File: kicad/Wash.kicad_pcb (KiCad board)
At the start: 4 copper layers, 55 x 35 mm, 40 parts, among them X2Y-CAN 4.7nF X2Y, X2Y-RS485 4.7nF X2Y

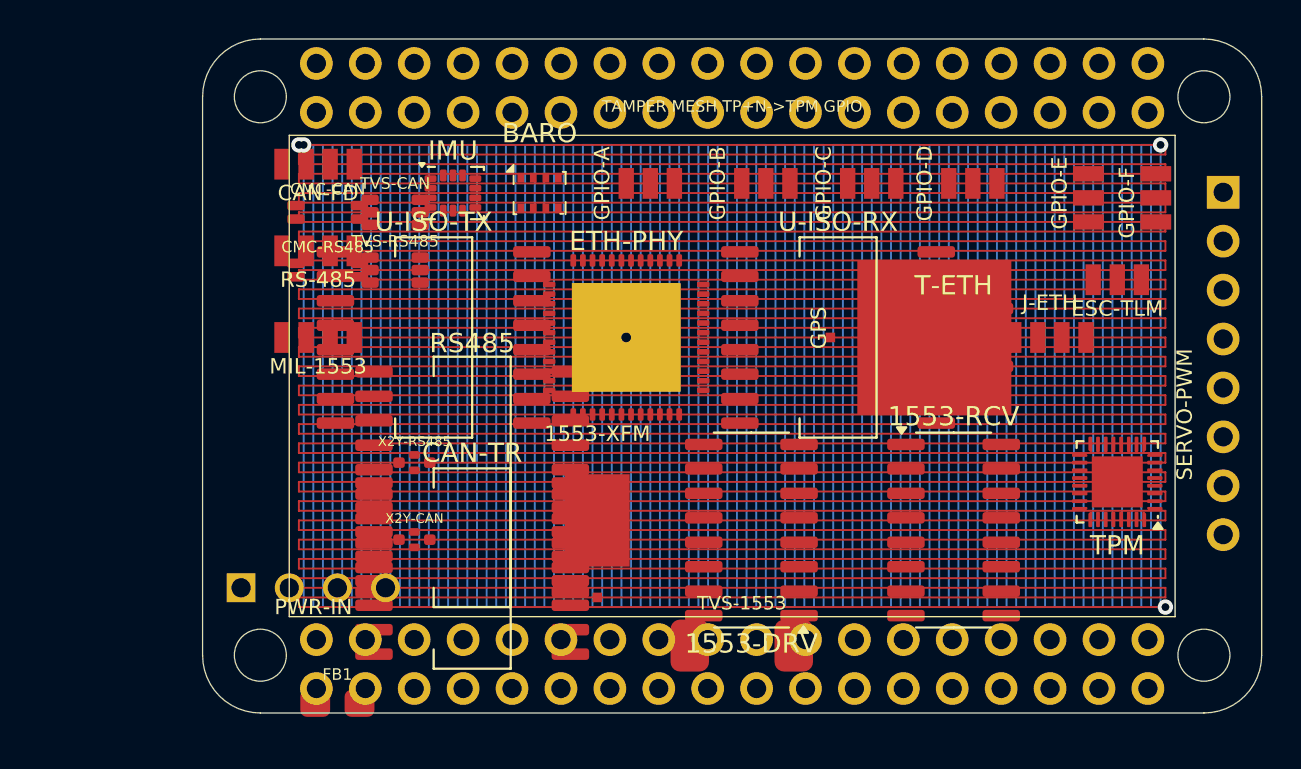
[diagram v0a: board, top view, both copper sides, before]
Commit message: avionics: wire second Ethernet (ETH2) on Wash; preserve Wash/Zoë layout work
Wash cape now carries a fully-wired second Ethernet channel.  The newly
placed ETH2 / ETH2-PHY (ADIN1300) / T-ETH2 (749010012A) footprints were
unconnected; this assigns their nets to mirror the ETH1 topology exactly:

  ETH2 (JST-GH-4P) --ETH2_LINE_{TX,RX}{P,N}--> T-ETH2 --ETH2_{TX,RX}{P,N}-->
  ETH2-PHY, reusing the host-side nets already broken out on the PB2-P2
  header (RMII1_* bus, shared MDIO/MDC, PHY2_INTRN/PHY2_RSTN, VCC2_ETH/
  GND/GND2_ETH).  44 pads assigned across the three parts (ETH2-PHY 32,
  T-ETH2 8, ETH2 4); diff-pair chains verified end to end.

Also preserves the manual component rearrangements on Wash and Zoë
(components reseated clear of the isolation moats).

Known follow-up (not in this commit): both PHYs share MDIO with no
address-strap resistors on the board (same default MDIO address); the
tamper-mesh shorts, ratsnest routing, and remaining DRC violations on all
four capes are still open.

Co-Authored-By: Claude Opus 4.8 <noreply@anthropic.com>
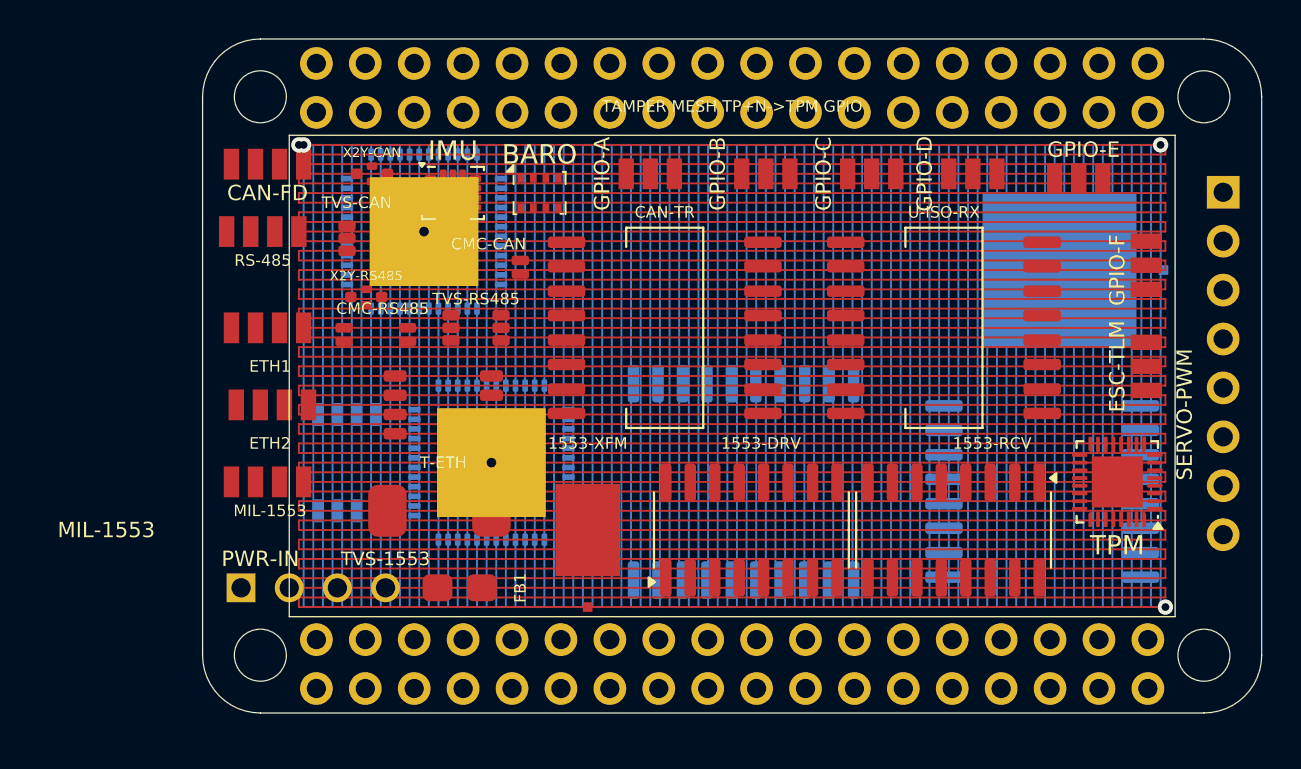
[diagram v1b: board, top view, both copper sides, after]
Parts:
- added ETH2: JST-GH-4P-ETH, JST_GH_4P, F.Cu at (124.6, 106.5)
- added ETH2-PHY: ADIN1300BCPZ, QFN-48-1EP_7x7mm_P0.5mm_EP5.65x5.65mm, B.Cu at (136.0, 109.5)
- added T-ETH2: 749010012A, ETH_XFMR_8P_5x3.5mm, B.Cu at (128.5, 109.5)
- ETH1-PHY: renamed from ETH-PHY; moved to B.Cu
- GPS, RS485, U-ISO-TX: moved to B.Cu
- moved ETH1 40.6 mm to (124.4, 102.5)
- moved U-ISO-TX 32.6 mm to (164.6, 111.0), turned to 180 degrees
- moved T-ETH 26.7 mm to (133.5, 106.5)
- moved X2Y-CAN 19.1 mm to (129.8, 94.5)
- moved TVS-1553 17.2 mm to (133.3, 112.0)
- moved CAN-TR 16.0 mm to (145.0, 102.5)
- moved RS485 14.1 mm to (149.1, 110.5), turned to -90 degrees
- moved ETH1-PHY 11.9 mm to (132.5, 97.5), turned to 180 degrees
- moved X2Y-RS485 8.96 mm to (129.5, 100.9)
- moved CMC-CAN 8.82 mm to (135.8, 99.3)
- moved FB1 8.74 mm to (134.3, 116.0)
- moved MIL-1553 7.95 mm to (124.4, 110.5)
- moved GPS 7.38 mm to (165.5, 99.5), turned to 180 degrees
- moved U-ISO-RX 5.52 mm to (159.5, 102.5)
- moved TVS-RS485 5.16 mm to (135.2, 102.5)
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- renumbered J-ETH to ETH1
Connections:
- CAN-TR pad 12: GND2_CAN -> (no net)
- CAN-TR pad 13: GND2_CAN -> (no net)
- CAN-TR pad 14: VCC2_CAN -> (no net)
- CAN-TR pad 9: CAN_H -> (no net)
- RS485 pad 11: VCC2_RS485 -> (no net)
- RS485 pad 12: GND2_RS485 -> (no net)
- RS485 pad 13: GND2_RS485 -> (no net)
- RS485 pad 14: RS485_A -> (no net)
- RS485 pad 18: GND2_RS485 -> (no net)
- RS485 pad 19: GND2_RS485 -> (no net)
- RS485 pad 20: VCC2_RS485 -> (no net)
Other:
- board text added: "MIL-1553"

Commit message: avionics(Wash): split PHY MDIO buses and wire field connectors
MDIO separation — each PB2-I NIC now manages its own PHY:
  * PHY1/ETH1-PHY -> MDIO0/MDC0 (CPSW MDIO, PB2-P2 pins 17/18)
  * PHY2/ETH2-PHY -> MDIO1/MDC1 (2nd bus, PB2-P2 pins 1/2 = spare SERVO6/7)
Removes the shared-MDIO same-address conflict (no strap needed). PCB pad
nets and schematic global labels both updated. PHY2's bus is a 2nd
(bit-banged mdio-gpio) MDIO — confirm the two balls are GPIO-capable in
the PB2-I pinmux and bring it up in the device tree.

Field connectors were all floating; wired each to its Description pinout:
  * SERVO-PWM pads 1-6 -> SERVO0-5 (servo PWM)
  * ESC-TLM -> GND / UART_ESC_TX / UART_ESC_RX
  * GPIO-A..F -> GND / +3V3 (+ GPIO_EXP_* signal pin labelled)
  * CAN-FD -> GND / CAN_H / CAN_L / +3V3
  * RS-485 -> GND / RS485_A / RS485_B / +3V3
  * PWR-IN -> +5V / +5V / GND / GND

The connector-vs-TMESH shorts DRC now reports are the pre-existing
tamper-mesh overlap (resolved by the per-domain mesh rework), not the
connector wiring.

Still open (need decisions, tracked in TODO 1.2a.1): source the 6
GPIO_EXP_A..F signals (PB2 header is full); add an ESC-PWM connector for
DSHOT0-3 (none on the PCB); wire MIL-1553 connector + transformer;
reconcile Wash.md §14 with the actual PCB connector set.

Co-Authored-By: Claude Opus 4.8 <noreply@anthropic.com>
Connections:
- CAN-FD pad 1: (no net) -> GND
- CAN-FD pad 2: (no net) -> CAN_H
- CAN-FD pad 3: (no net) -> CAN_L
- CAN-FD pad 4: (no net) -> +3V3
- ESC-TLM pad 1: (no net) -> GND
- ESC-TLM pad 2: (no net) -> UART_ESC_TX
- ESC-TLM pad 3: (no net) -> UART_ESC_RX
- ETH1-PHY pad 18: MDIO -> MDIO0
- ETH1-PHY pad 19: MDC -> MDC0
- ETH2-PHY pad 18: MDIO -> MDIO1
- ETH2-PHY pad 19: MDC -> MDC1
- GPIO-A pad 1: (no net) -> GND
- GPIO-A pad 2: (no net) -> +3V3
- GPIO-A pad 3: (no net) -> GPIO_EXP_A
- GPIO-B pad 1: (no net) -> GND
- GPIO-B pad 2: (no net) -> +3V3
- GPIO-B pad 3: (no net) -> GPIO_EXP_B
- GPIO-C pad 1: (no net) -> GND
- GPIO-C pad 2: (no net) -> +3V3
- GPIO-C pad 3: (no net) -> GPIO_EXP_C
- GPIO-D pad 1: (no net) -> GND
- GPIO-D pad 2: (no net) -> +3V3
- GPIO-D pad 3: (no net) -> GPIO_EXP_D
- GPIO-E pad 1: (no net) -> GND
- GPIO-E pad 2: (no net) -> +3V3
- GPIO-E pad 3: (no net) -> GPIO_EXP_E
- GPIO-F pad 1: (no net) -> GND
- GPIO-F pad 2: (no net) -> +3V3
- GPIO-F pad 3: (no net) -> GPIO_EXP_F
- PB2-P2 pad 1: SERVO7 -> MDIO1
- PB2-P2 pad 17: MDIO -> MDIO0
- PB2-P2 pad 18: MDC -> MDC0
- PB2-P2 pad 2: SERVO6 -> MDC1
- PWR-IN pad 1: (no net) -> +5V
- PWR-IN pad 2: (no net) -> +5V
- PWR-IN pad 3: (no net) -> GND
- PWR-IN pad 4: (no net) -> GND
- RS-485 pad 1: (no net) -> GND
- RS-485 pad 2: (no net) -> RS485_A
- RS-485 pad 3: (no net) -> RS485_B
- RS-485 pad 4: (no net) -> +3V3
- SERVO-PWM pad 1: (no net) -> SERVO0
- SERVO-PWM pad 2: (no net) -> SERVO1
- SERVO-PWM pad 3: (no net) -> SERVO2
- SERVO-PWM pad 4: (no net) -> SERVO3
- SERVO-PWM pad 5: (no net) -> SERVO4
- SERVO-PWM pad 6: (no net) -> SERVO5

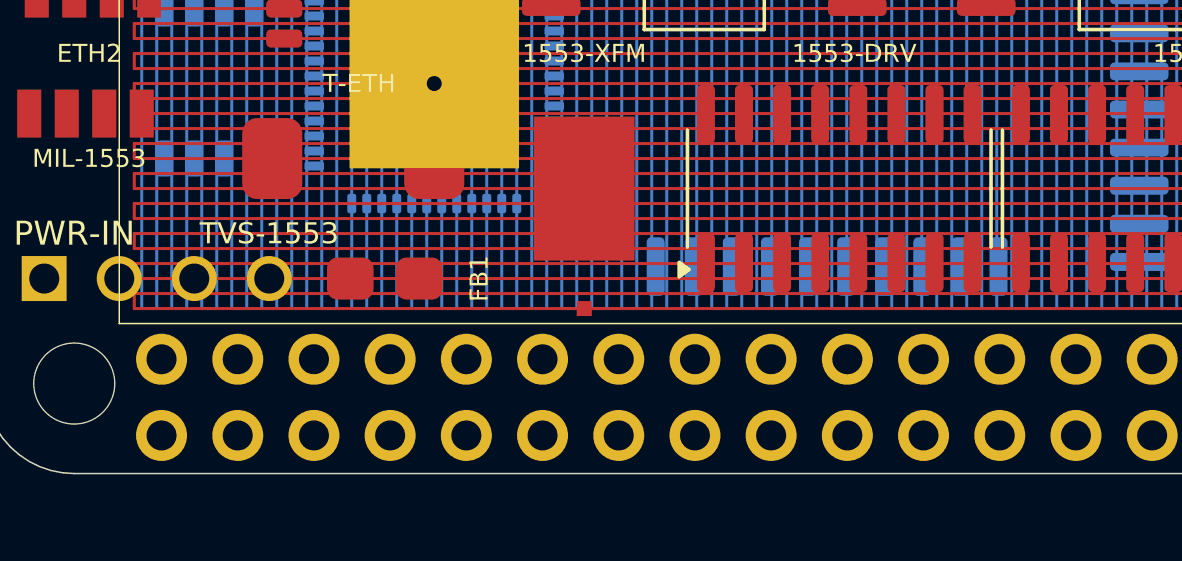
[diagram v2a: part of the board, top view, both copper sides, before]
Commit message: avionics(Wash): add I2C GPIO expander and ESC-PWM connector
Resolves the two open I/O gaps from the connector-wiring pass:

* U-GPIO (PCA9555DB, SSOP-24, I2C addr 0x20) + C-GPIO 100nF decoupling.
  P0_0..P0_5 -> GPIO_EXP_A..F now source the six GPIO-A..F expansion
  connectors over the existing I2C1 bus (no SoC pins consumed). A0/A1/A2
  to GND; INT and the spare P0_6/P0_7 + P1_x left NC.
* ESC-PWM (JST-GH SM05B, 5-pin): pins 1-4 -> DSHOT0..3, pin 5 -> GND,
  giving the four EDF ESC/BDSHOT PWM outputs a connector to the nacelle
  harness.

GPIO_EXP_A..F, DSHOT0..3, and I2C1_SCL/SDA are now 2-pad (fully netted).
New parts placed at tentative locations for the user to finalise; I2C1
pull-ups to verify. Tracked in TODO 1.2a.1.

Co-Authored-By: Claude Opus 4.8 <noreply@anthropic.com>
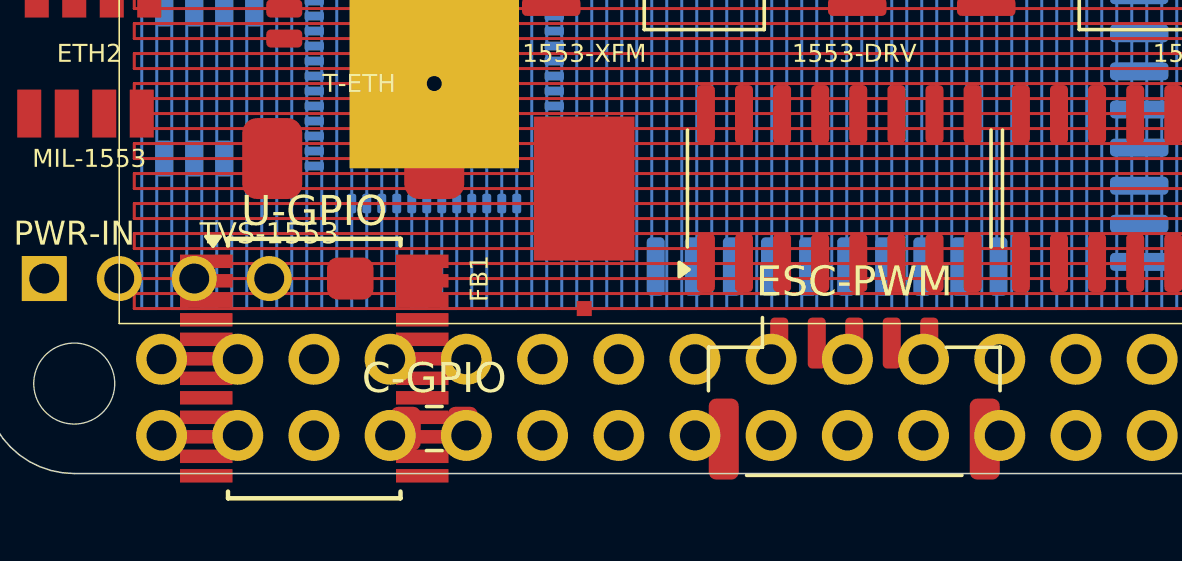
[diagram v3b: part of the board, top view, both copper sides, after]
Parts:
- added C-GPIO: 100nF, C_0805_2012Metric, F.Cu at (136.0, 121.0)
- added ESC-PWM: JST-GH-5P-ESC, JST_GH_SM05B-GHS-TB_1x05-1MP_P1.25mm_Horizontal, F.Cu at (150.0, 120.0)
- added U-GPIO: PCA9555DB, SSOP-24_5.3x8.2mm_P0.65mm, F.Cu at (132.0, 119.0)
